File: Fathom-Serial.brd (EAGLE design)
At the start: 112.4 x 45.7 mm, 115 parts, among them IC1 LMH6643, IC2 LMH6643, IC3 ST490AB, IC4 ST490AB, IC5 FT230XS, Q1 BC817-40W, U1 MC7812, U2 MC7805, U4 INA139, U5 MC7805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

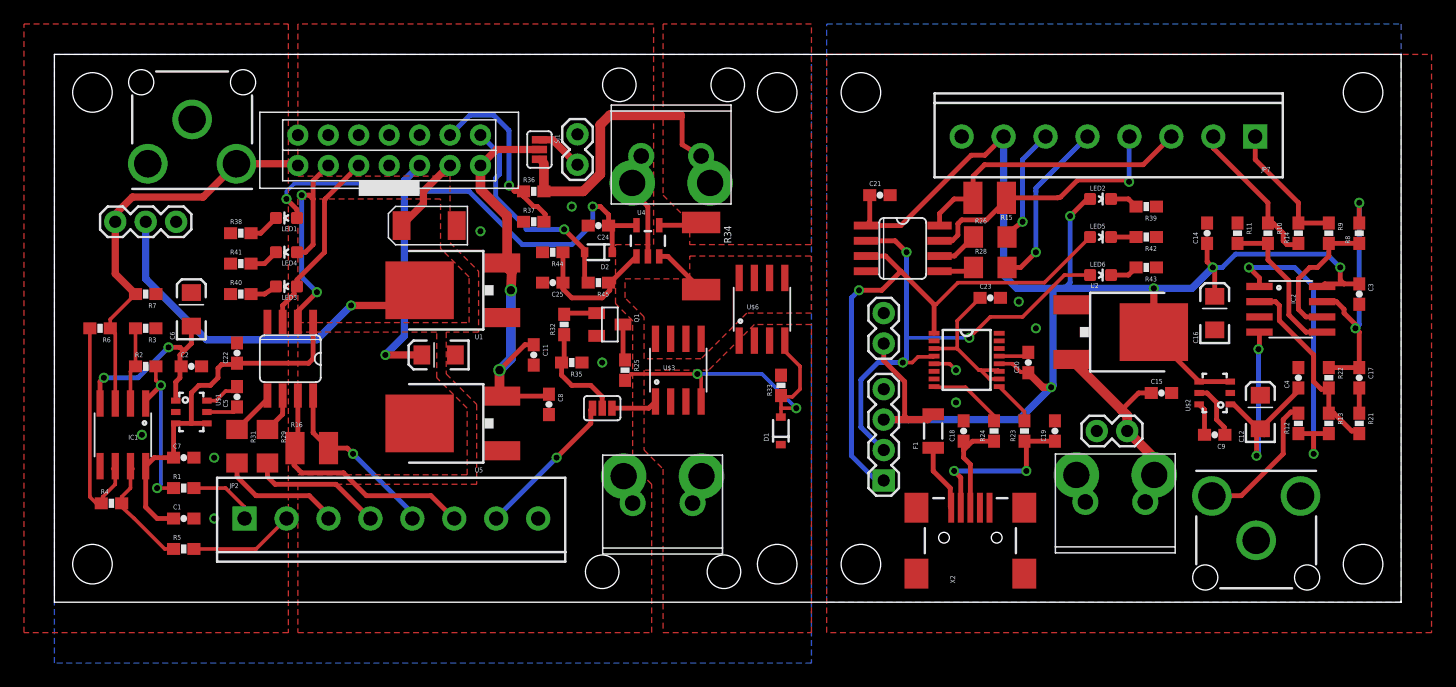
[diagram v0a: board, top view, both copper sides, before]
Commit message: Lots of changes based on testing of first prototype. Fixed regulators, removed RX/TX leds, added RTS reset, changed negative supply capacitors.
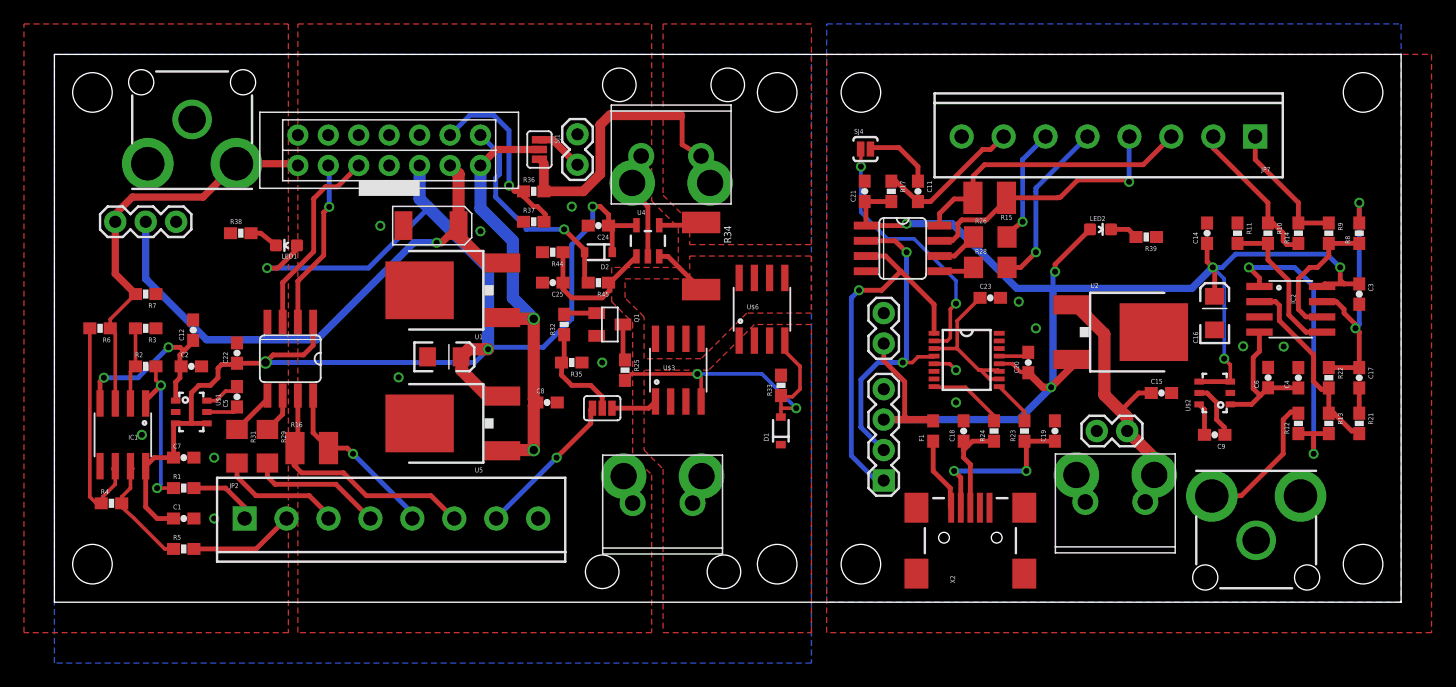
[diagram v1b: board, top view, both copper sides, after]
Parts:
- removed LED3, LED4, LED5, LED6: YELLOW, SparkFun-LED:LED-0603
- removed R40, R41, R42, R43: 1K, SparkFun-Resistors:0603-RES
- added R17: 10K, SparkFun:0603-RES
- added SJ4: JUMPER-PAD-2-NC_BY_PASTE, SparkFun-Passives:PAD-JUMPER-2-NC_BY_PASTE_YES_SILK
- C11: value 0.1uF -> 1uF; device SparkFun-Passives:0603-CAP -> SparkFun:0603-CAP
- C12, C6: value 2.2uF -> 2.2uF X5R; device SparkFun-Passives:EIA3216 -> SparkFun-Passives:0603-CAP
- C14, C7: value 0.1uF -> 2.2uF X5R
- C5, C9: value 1uF -> 1uF X5R
- F1: device SparkFun:PTC-1206 -> SparkFun:0603
- JP1, JP6: device SparkFun-Connectors:RCA -> BR-Eagle-Library:RCA
- U1, U2, U5: device SparkFun-PowerIC:DPAK -> BR-Eagle-Library:DPAK
- moved C6 90.0 mm to (101.3, 18.7)
- moved C12 89.3 mm to (11.6, 22.7)
- moved C11 34.9 mm to (72.1, 34.3)
- moved LED2 2.54 mm to (87.3, 31.1)
- moved R39 2.54 mm to (91.1, 30.5)
- moved LED1 2.29 mm to (19.4, 29.8)
- moved C21 1.31 mm to (67.6, 34.3), turned to 90 degrees
- moved C10 0.50 mm to (32.5, 20.5), turned to 0 degrees
- moved C8 0.22 mm to (41.1, 16.7), turned to 0 degrees
- moved C13 0.16 mm to (31.4, 31.4), turned to 180 degrees
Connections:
- removed net N$34: LED3.C, R40.2
- removed net N$35: LED4.C, R41.2
- removed net N$36: LED5.C, R42.2
- removed net N$37: LED6.C, R43.2
- new net N$7: C11.1, SJ4.2
- new net ROV-ON-CTRL: C11.2, JP7.7, R17.1
- new net RTS: IC5.2, SJ4.1
- net -VCC: now also C6.1; no longer C12.C
- net -VCC-ISO: now also C12.1; no longer C6.C
- net 12V-ISO: now also U1.3; no longer U1.4
- net GND: now also C6.2, U2.4; no longer C12.A, R42.1, R43.1, U2.1
- net GND-ISO: now also C12.2, U1.4, U5.4; no longer C11.2, C6.A, R40.1, R41.1, U1.1, U5.1
- net ROV-RX: no longer LED4.A
- net ROV-TX: no longer LED3.A
- net ROV-VIN: now also U1.1, U5.1; no longer C11.1, U1.3, U5.3
- net RX-I: no longer LED6.A
- net TOP-VIN: now also U2.1; no longer U2.3
- net TX-O: no longer LED5.A
- net VCC: now also R17.2, U2.3; no longer JP7.7, U2.4
- net VCC-ISO: now also U5.3; no longer U5.4
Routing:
- net VCC-ISO: track 91.3 -> 120.1 mm, vias 3 -> 4
- net RTS: track 0.00 -> 22.2 mm, vias 0 -> 2
- net RX-I: track 44.2 -> 26.7 mm, vias 3 -> 2
- net TX-O: track 46.9 -> 31.5 mm
- net ROV-ON-CTRL: track 0.00 -> 12.3 mm
- net -VCC: track 22.0 -> 12.3 mm, vias 2 -> 0
- net 12V-ISO: track 38.0 -> 47.7 mm
- net VCC: track 128.9 -> 119.3 mm, vias 5 -> 6
- net ROV-RX: track 21.6 -> 14.2 mm, vias 2 -> 1
- net N$7: track 0.00 -> 5.89 mm
- net TOP-VIN: track 18.1 -> 23.7 mm
- net N$35: track 2.48 -> 0.00 mm
- net N$37: track 2.35 -> 0.00 mm
- net N$34: track 2.28 -> 0.00 mm
- net N$36: track 2.08 -> 0.00 mm
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- removed copper zone on layer 1, net 12V-ISO
- removed copper zone on layer 1, net VCC-ISO
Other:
- board text added: "FATHOM-ROV-INTERFACE rev2"
- board text added: "FATHOM-TOPSIDE-INTERFACE rev2"
- board text added: "RTS RESET"
- board text removed: "FATHOM-ROV-INTERFACE rev1"
- board text removed: "FATHOM-TOPSIDE-INTERFACE rev1"
